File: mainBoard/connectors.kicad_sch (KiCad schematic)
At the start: 51 parts, among them J10 Conn_01x06, J11 Conn_01x07, J12 Conn_01x04, J13 Conn_01x04, J15 Conn_02x05_Odd_Even, J16 Conn_01x02, J17 Conn_01x05, J7 Conn_01x02, J8 Conn_01x02, J9 Conn_01x02, K1 Relay_SPDT, Q3 IRLML6244TRPBF, Q4 IRLML6244TRPBF, Q5 IRLML6244TRPBF, Q6 IRLML6244TRPBF, Q7 IRLML6244TRPBF, U16 100, U17 100, U18 USBLC6-2SC6, U19 USBLC6-4SC6, U21 100, U22 USBLC6-4SC6, U23 USBLC6-4SC6, U24 USBLC6-4SC6, U25 USBLC6-4SC6

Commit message: Nearly finished with board after revisions
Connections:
- net +12V: now also J8.2 (Pin_2), J9.2 (Pin_2); no longer J8.1 (Pin_1), J9.1 (Pin_1)
- net ESD_PB12: now also U21.1; no longer U21.7
- net ESD_PB13: now also U21.3; no longer U21.5
- net ESD_PB14: now also U21.5; no longer U21.3
- net ESD_PB15: now also U21.7; no longer U21.1
- net FAN2_MINUS: now also J8.1 (Pin_1); no longer J8.2 (Pin_2)
- net FAN3_MINUS: now also J9.1 (Pin_1); no longer J9.2 (Pin_2)
- net KP_Col0: now also U17.5; no longer U17.6
- net KP_Col1: now also U17.3; no longer U17.4
- net KP_Col2: now also U17.1; no longer U17.2
- net KP_ESD_C0: now also U17.6; no longer U17.5
- net KP_ESD_C1: now also U17.4; no longer U17.3
- net KP_ESD_C2: now also U17.2; no longer U17.1
- net KP_ESD_R1: now also U16.6, U22.3 (I/O2); no longer U16.5, U22.1 (I/O1)
- net KP_ESD_R2: now also U16.4, U22.4 (I/O3); no longer U16.3, U22.3 (I/O2)
- net KP_ESD_R3: now also U16.2, U22.6 (I/O4); no longer U16.1, U22.4 (I/O3)
- net KP_ESD_R30: now also U16.8, U22.1 (I/O1); no longer U16.7, U23.6 (I/O4)
- net KP_Row0: now also U16.7; no longer U16.8
- net KP_Row1: now also U16.5; no longer U16.6
- net KP_Row2: now also U16.3; no longer U16.4
- net KP_Row3: now also U16.1; no longer U16.2
- net PB12: now also U21.2; no longer U21.8
- net PB13: now also U21.4; no longer U21.6
- net PB14: now also U21.6; no longer U21.4
- net PB15: now also U21.8; no longer U21.2
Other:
- moved on the sheet: J11, U16, U17, U22, U23

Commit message: work on AC power side
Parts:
- J16: footprint TerminalBlock_Phoenix:TerminalBlock_Phoenix_MKDS-1,5-2-5.08_1x02_P5.08mm_Horizontal -> PhoenixContact_MKDS_9mm:CONN_1714971_PXC
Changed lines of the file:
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@@
 			)
 		)
-		(property "Footprint" "TerminalBlock_Phoenix:TerminalBlock_Phoenix_MKDS-1,5-2-5.08_1x02_P5.08mm_Horizontal"
+		(property "Footprint" "PhoenixContact_MKDS_9mm:CONN_1714971_PXC"
 			(at 210.82 102.87 0)
 			(hide yes)

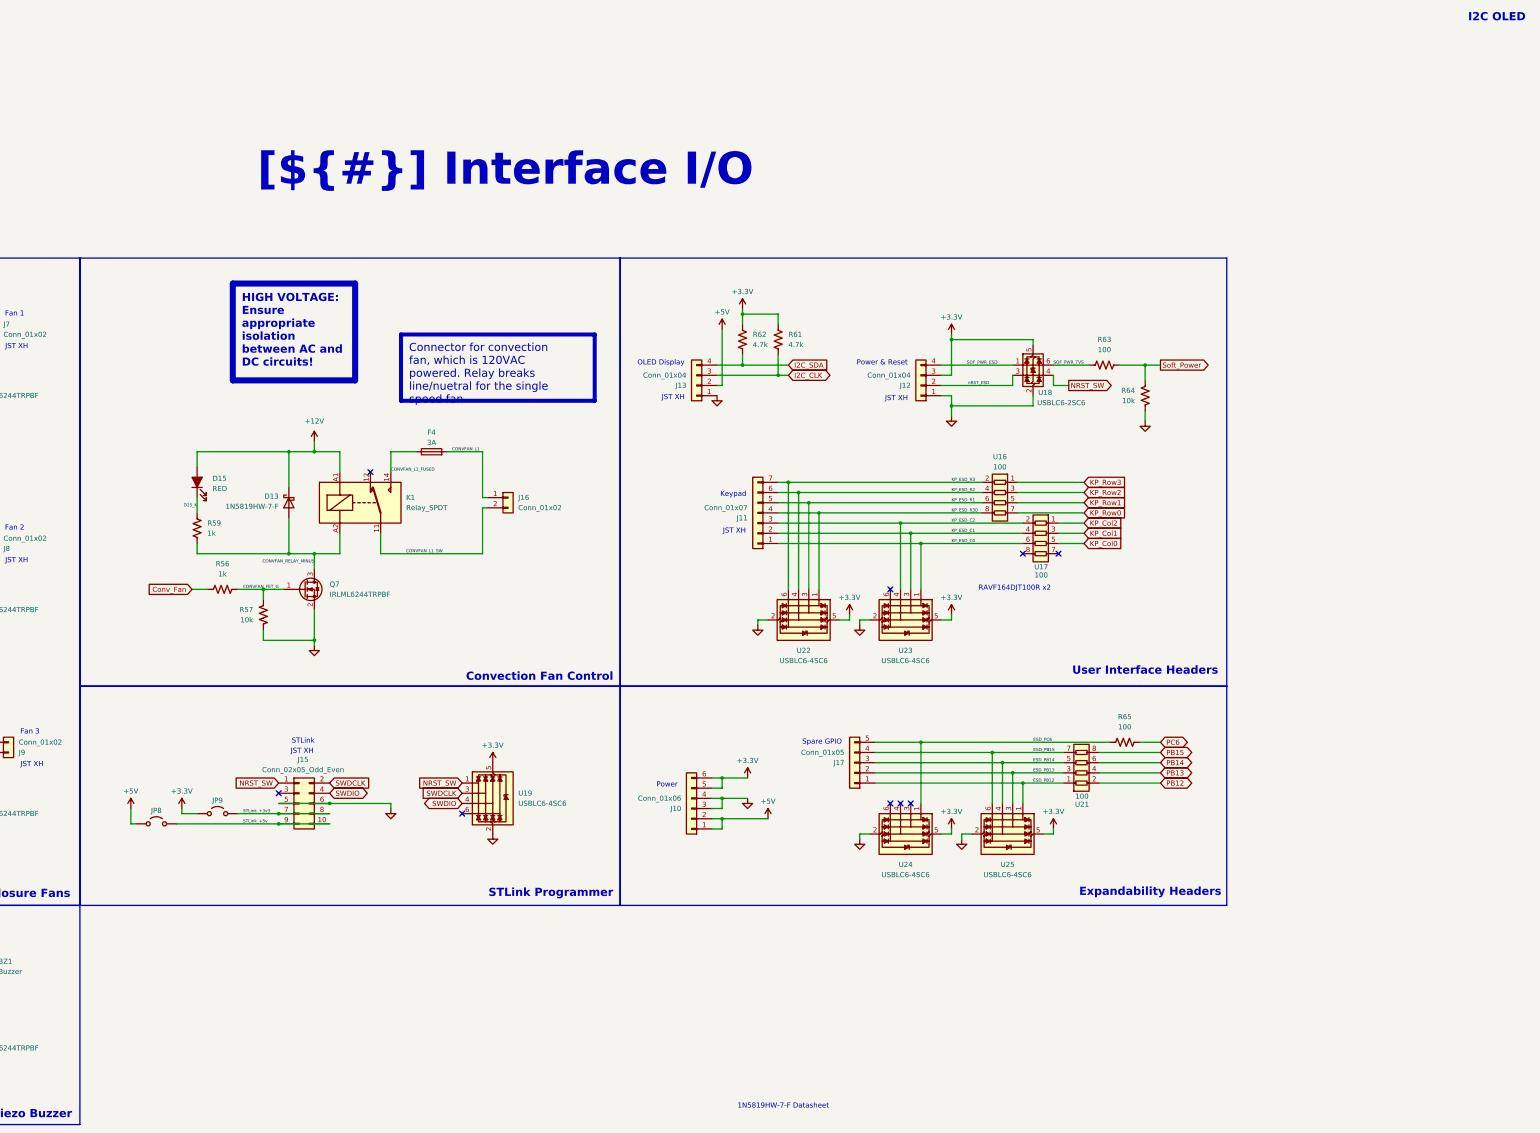
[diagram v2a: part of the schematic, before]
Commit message: add USB-A and change capacitors
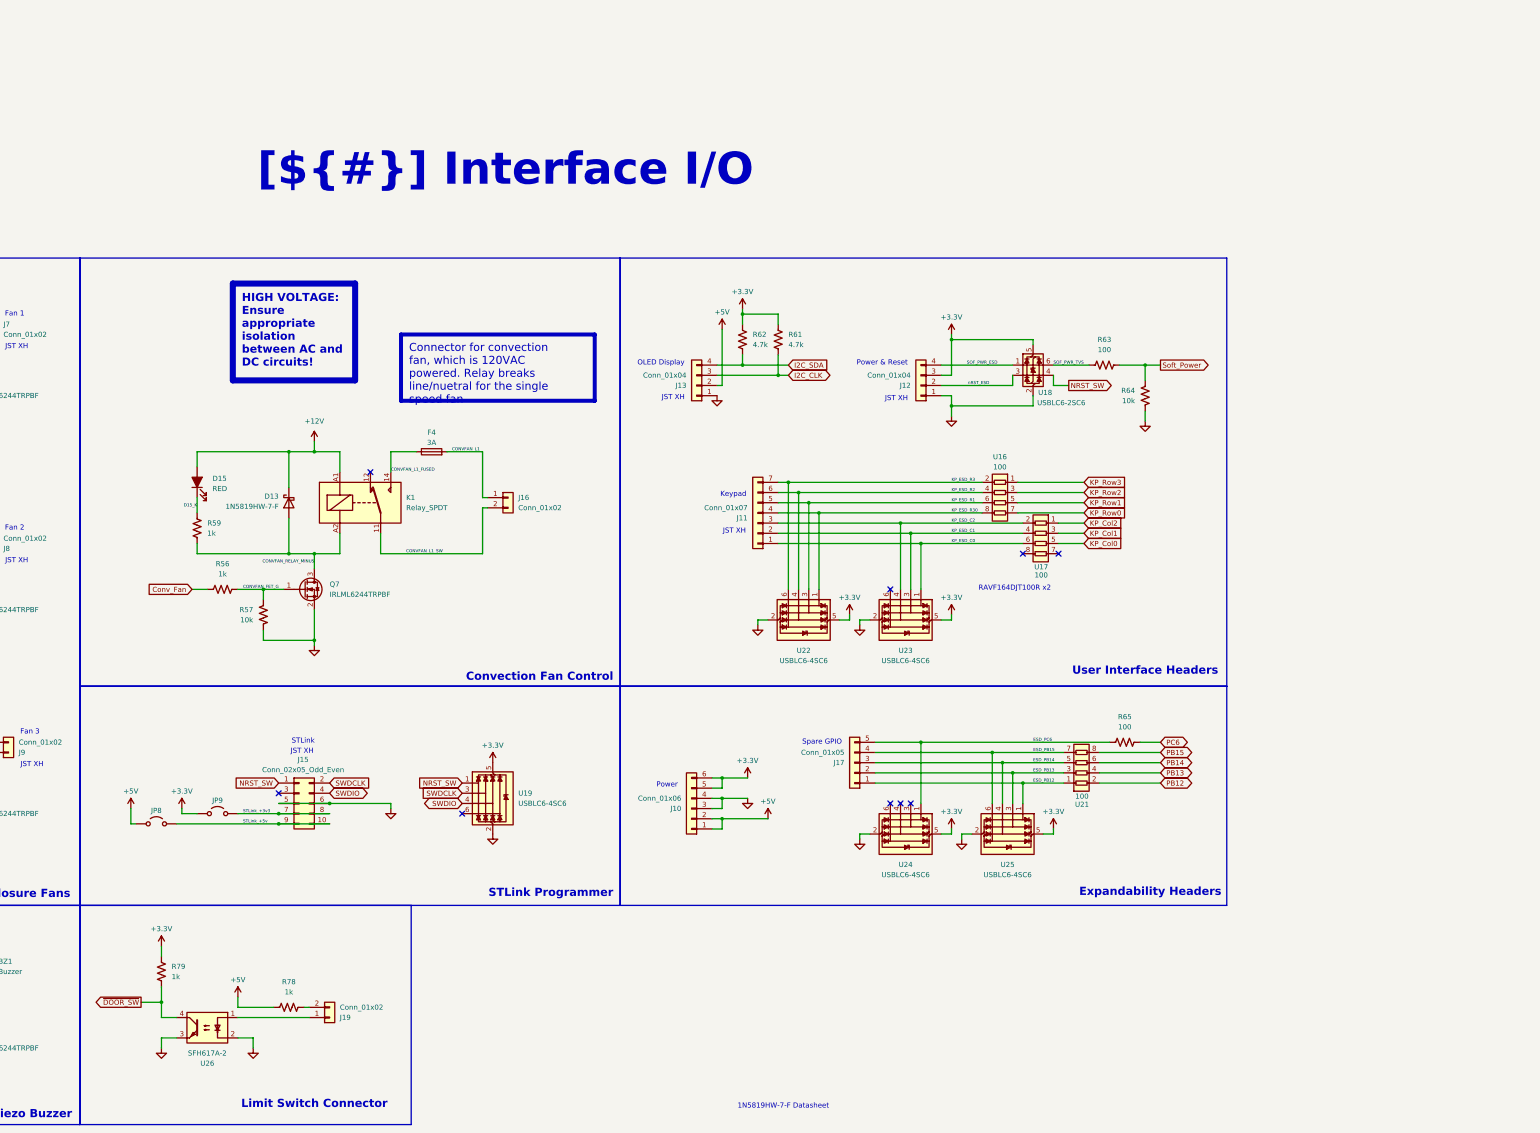
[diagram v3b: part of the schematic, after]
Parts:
- added J19: Conn_01x02, TerminalBlock_Phoenix:TerminalBlock_Phoenix_MKDS-1,5-2-5.08_1x02_P5.08mm_Horizontal, symbol Connector_Generic:Conn_01x02
- added R78, R79: 1k, Resistor_SMD:R_0603_1608Metric_Pad0.98x0.95mm_HandSolder, symbol Device:R_US
- added U26: SFH617A-2, Package_DIP:DIP-4_W7.62mm, symbol Isolator:SFH617A-2
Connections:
- net +3.3V: now also R79.1
- net +5V: now also R78.2
- net GND: now also U26.2, U26.3
- new net: J19.1 (Pin_1), U26.1
- new net: J19.2 (Pin_2), R78.1
- new net ~{DOOR_SW}: R79.2, U26.4
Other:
- note added: "Limit Switch Connector"
- note removed: "I2C OLED"

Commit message: change to single 4" touchscreen for UI instead of keypad and buttons
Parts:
- removed J11: Conn_01x07, Connector_JST:JST_XH_B7B-XH-A_1x07_P2.50mm_Vertical, symbol Connector_Generic:Conn_01x07
- removed J13: Conn_01x04, Connector_JST:JST_XH_B4B-XH-A_1x04_P2.50mm_Vertical, symbol Connector_Generic:Conn_01x04
- removed R61, R62: 4.7k, Resistor_SMD:R_0603_1608Metric_Pad0.98x0.95mm_HandSolder, symbol Device:R_US
- removed U16, U17: 100, Resistor_SMD:R_Array_Convex_4x1206, symbol Parallel_Resistor:ParallelArray-4
- removed U22, U23: USBLC6-4SC6, Package_TO_SOT_SMD:SOT-23-6, symbol Power_Protection:USBLC6-4SC6
- added J19: Conn_01x14, Connector_JST:JST_XH_B14B-XH-A_1x14_P2.50mm_Vertical, symbol Connector_Generic:Conn_01x14
- added JP13: Jumper_3_Open, Jumper:SolderJumper-3_P1.3mm_Open_RoundedPad1.0x1.5mm, symbol Jumper:Jumper_3_Open
- added Q8: PMOS, symbol Simulation_SPICE:PMOS
- added R84: 10k, Resistor_SMD:R_0603_1608Metric_Pad0.98x0.95mm_HandSolder, symbol Device:R_US
- added U27, U28, U29: 100, Resistor_SMD:R_Array_Convex_4x1206, symbol Parallel_Resistor:ParallelArray-4
- added U30, U31: 74LVC1T45W6-7, Package_TO_SOT_SMD:SOT-23-6, symbol Logic_LevelTranslator:SN74LVC1T45DBV
- renumbered D10 to D12, D11 to D13, D12 to D14, D13 to D16, F4 to F2, J9 to J10, J15 to J11, J19 to J12, J16 to J13, J10 to J14, J12 to J18, J7 to J8, J8 to J9, JP8 to JP11, JP9 to JP12, R47 to R65, R48 to R66, R49 to R67, R50 to R68, R51 to R69, R52 to R70, R53 to R71, R54 to R72, R55 to R73, R79 to R74, R59 to R75, R56 to R76, R57 to R77, R63 to R81, R65 to R82, R64 to R83, U26 to U17, U19 to U18, U24 to U21, U25 to U23, U18 to U24, U21 to U26
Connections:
- net +3.3V: now also J18.4 (Pin_4), JP13.3 (B), U30.1 (VCCA), U31.1 (VCCA); no longer J18.3 (Pin_3)
- net +5V: now also JP13.1 (A), Q8.1 (D), R84.2
- net GND: now also J19.2 (Pin_2), U30.2 (GND), U30.5 (DIR), U31.2 (GND), U31.5 (DIR)
- net SOF_PWR_ESD: now also J18.3 (Pin_3); no longer J18.4 (Pin_4)
- net ~{DOOR_SW} renamed DOOR_SW
- new net: J19.11 (Pin_11), U28.1
- new net: J19.10 (Pin_10), U28.3
- new net: J19.9 (Pin_9), U28.5
- new net: U28.6, U30.4 (B)
- new net: J19.7 (Pin_7), U28.7
- new net: U29.6, U31.4 (B)
- new net: Q8.2 (G), R84.1, U29.1
- new net: J19.14 (Pin_14), U29.3
- new net: J19.13 (Pin_13), U29.5
- new net: J19.12 (Pin_12), U29.7
- new net: J19.3 (Pin_3), U27.1
- new net: J19.4 (Pin_4), U27.3
- new net: J19.5 (Pin_5), U27.5
- new net: J19.6 (Pin_6), U27.7
- new net LCD_BL: U29.2
- new net LCD_Backlight: J19.8 (Pin_8), Q8.3 (S)
- new net LCD_CS: U27.2
- new net LCD_MISO: U30.3 (A)
- new net LCD_MOSI: U27.8
- new net LCD_RS: U27.6
- new net LCD_RST: U27.4
- new net LCD_SCK: U28.8
- new net Touch_CS: U28.2
- new net Touch_IRQ: U29.4
- new net Touch_MISO: U31.3 (A)
- new net Touch_MOSI: U29.8
- new net Touch_SCK: U28.4
- new net VAA: J19.1 (Pin_1), JP13.2 (C), U30.6 (VCCB), U31.6 (VCCB)
- no-connect marks 9 -> 6
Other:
- note added: "4.0" Touch LCD"
- note added: "External Power/Reset Buttons"
- note removed: "Keypad"
- note removed: "OLED Display"
- note removed: "RAVF164DJT100R x2"
- note removed: "User Interface Headers"
- moved on the sheet: BZ1, D12, D13, D14, D15, D16, F2, J10, J11, J12, J13, J14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

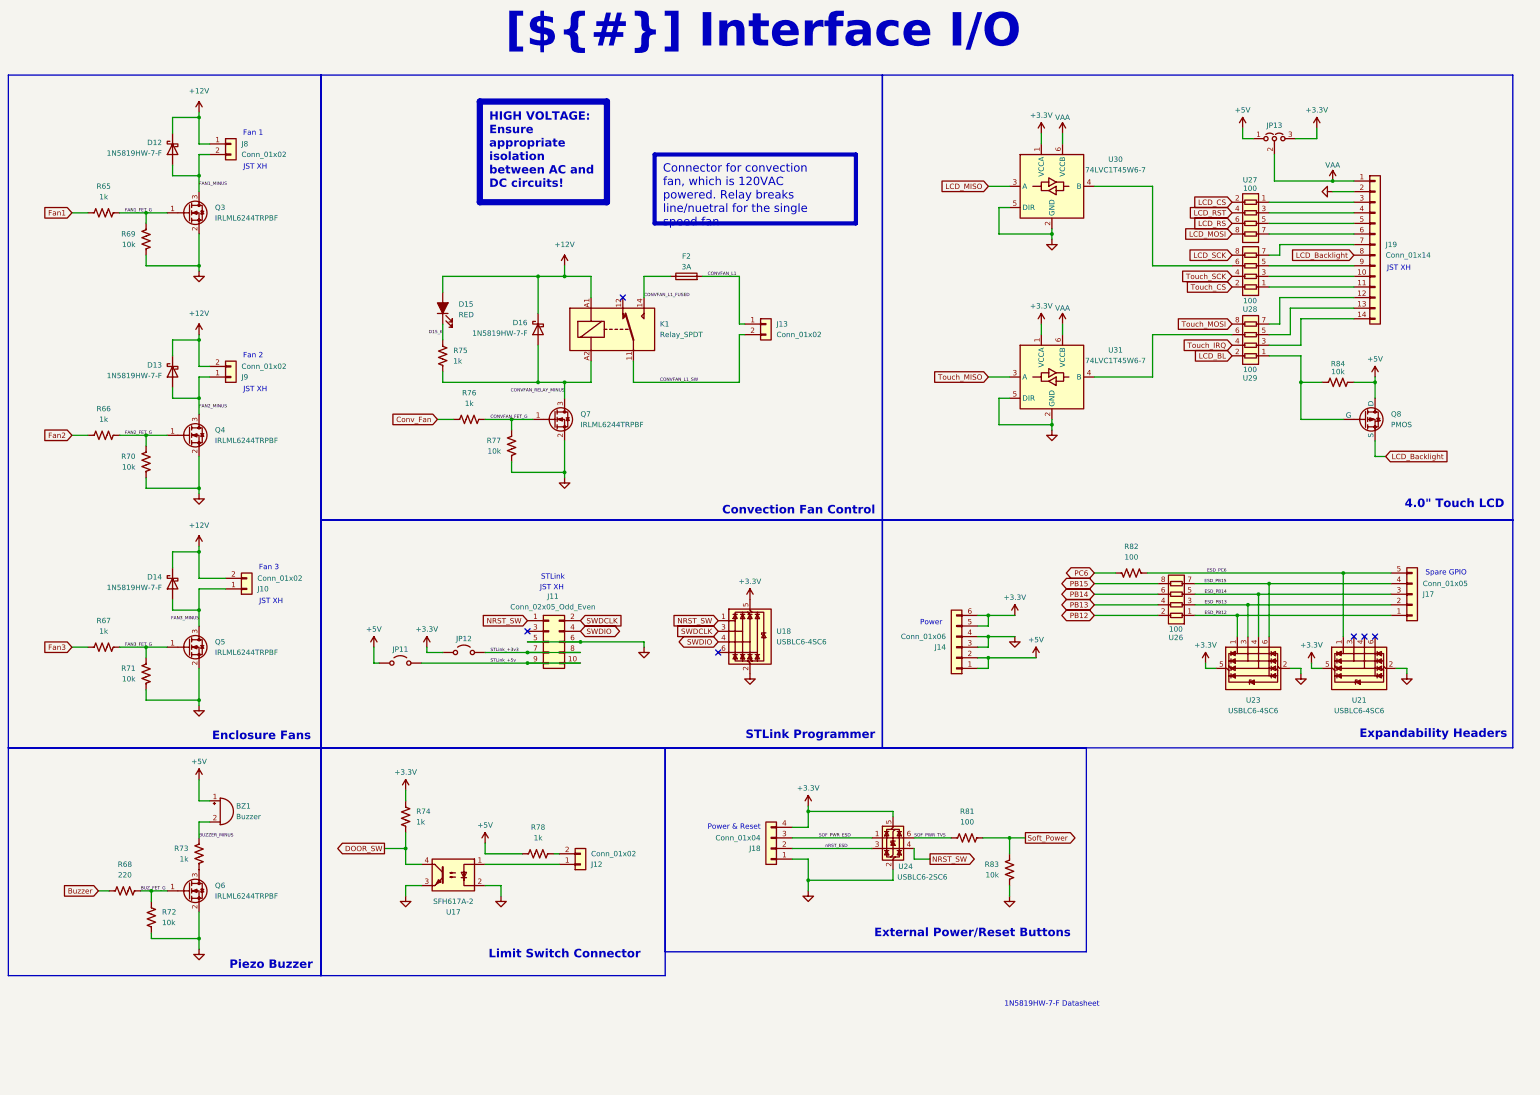
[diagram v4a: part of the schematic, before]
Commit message: change to stm32f413 and add a QSPI SRAM
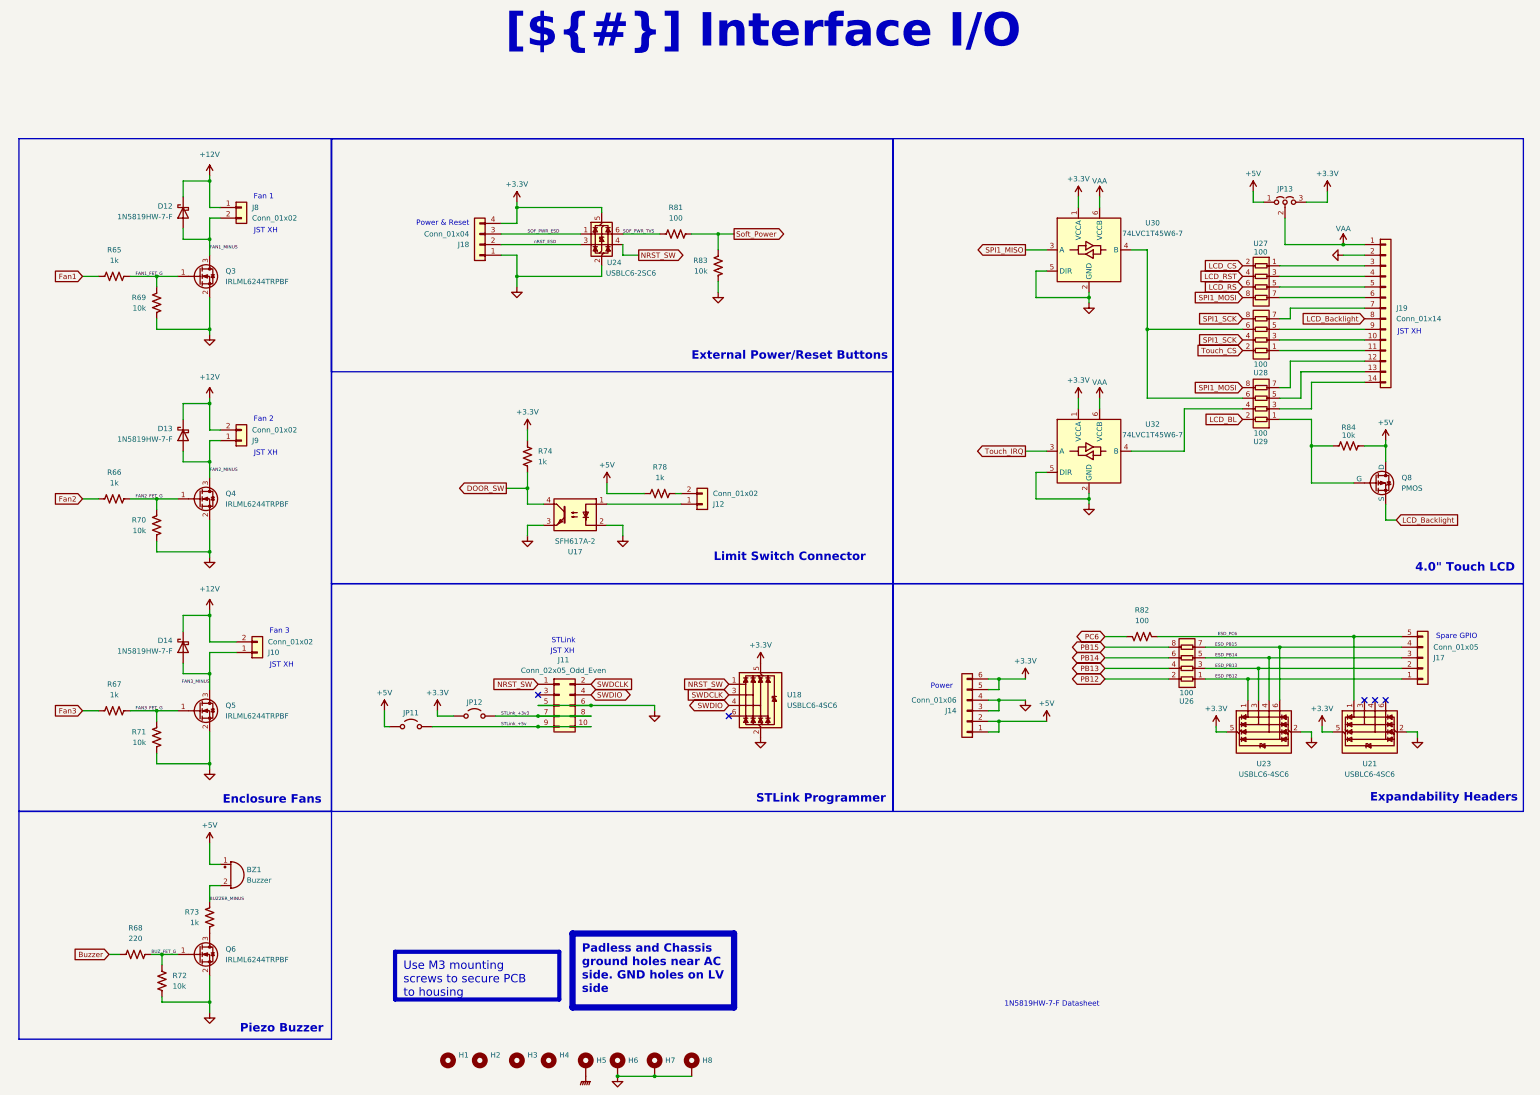
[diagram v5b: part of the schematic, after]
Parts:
- removed D15: RED, LED_SMD:LED_0603_1608Metric_Pad1.05x0.95mm_HandSolder, symbol Device:LED_Filled
- removed D16: 1N5819HW-7-F, Diode_SMD:D_SOD-123, symbol Diode:1N5819
- removed F2: 3A, Fuse:Fuseholder_Clip-5x20mm_Littelfuse_100_Inline_P20.50x4.60mm_D1.30mm_Horizontal, symbol Device:Fuse
- removed J13: Conn_01x02, PhoenixContact_MKDS_9mm:CONN_1714971_PXC, symbol Connector_Generic:Conn_01x02
- removed K1: Relay_SPDT, Relay_THT:Relay_SPDT_Finder_36.11, symbol Relay:Relay_SPDT
- removed Q7: IRLML6244TRPBF, Package_TO_SOT_SMD:SOT-23, symbol Transistor_FET:IRLML6244
- removed R75, R76: 1k, Resistor_SMD:R_0603_1608Metric_Pad0.98x0.95mm_HandSolder, symbol Device:R_US
- removed R77: 10k, Resistor_SMD:R_0603_1608Metric_Pad0.98x0.95mm_HandSolder, symbol Device:R_US
- removed U31: 74LVC1T45W6-7, Package_TO_SOT_SMD:SOT-23-6, symbol Logic_LevelTranslator:SN74LVC1T45DBV
- added H1, H2, H3, H4: MountingHole, MountingHole:MountingHole_3.2mm_M3, symbol Mechanical:MountingHole
- added H5, H6, H7, H8: MountingHole_Pad, MountingHole:MountingHole_3.2mm_M3_Pad_Via, symbol Mechanical:MountingHole_Pad
- added U32: 74LVC1T45W6-7, Package_TO_SOT_SMD:SOT-23-6, symbol Logic_LevelTranslator:SN74LVC1T45DBV
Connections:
- net Touch_MOSI is gone; now on net SPI1_MOSI: U29.8
- net Touch_SCK is gone; now on net SPI1_SCK: U28.4
- net +3.3V: now also U32.1 (VCCA)
- net GND: now also H6.1, H7.1, H8.1, U32.2 (GND), U32.5 (DIR)
- net Touch_IRQ: now also U32.3 (A); no longer U29.4
- net VAA: now also U32.6 (VCCB)
- net at U28.6, U30.4 (B): now also U29.6
- net LCD_MISO renamed SPI1_MISO
- net LCD_MOSI renamed SPI1_MOSI
- net LCD_SCK renamed SPI1_SCK
- new net: U29.4, U32.4 (B)
- new net GNDPWR: H5.1
- no-connect marks 6 -> 5
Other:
- note removed: "Convection Fan Control"
- moved on the sheet: BZ1, D12, D13, D14, J10, J11, J12, J14, J17, J18, J19, J8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
